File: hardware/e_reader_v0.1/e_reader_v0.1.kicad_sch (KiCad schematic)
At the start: 6 parts, among them J1 SD_Card, J2 Waveshare_7.5_EPD, J3 5Way_Joystick, U1 ESP32-S3-DevKitC

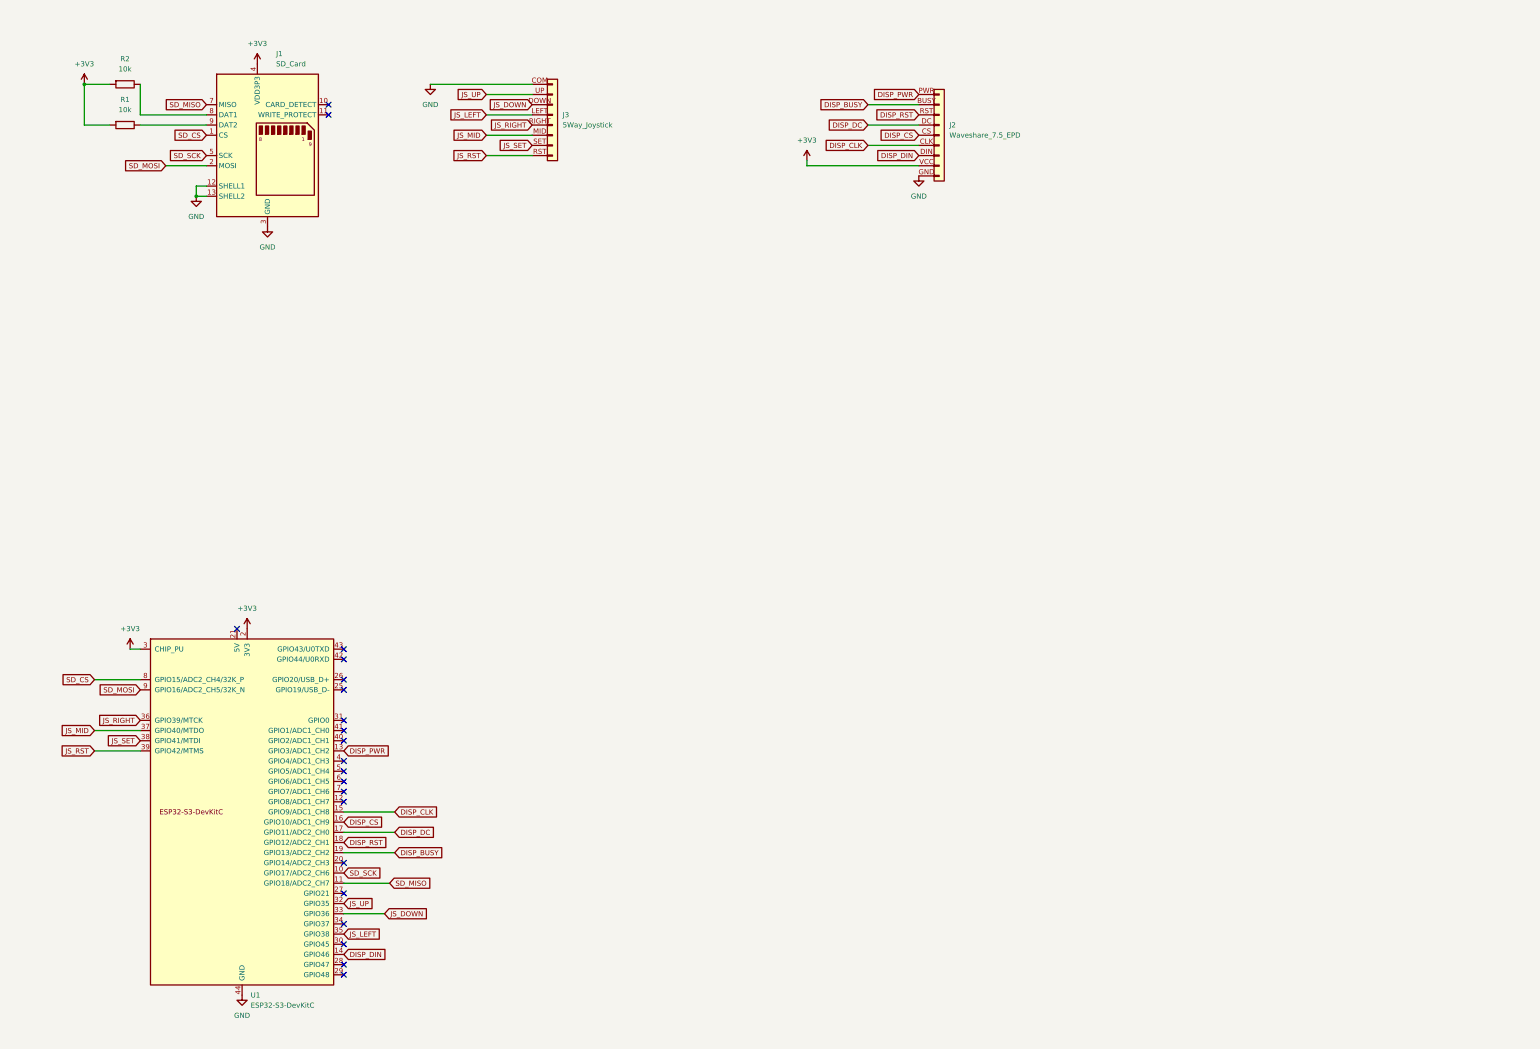
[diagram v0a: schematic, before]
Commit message: Add schematic v0.1 with power, display, SD, buttons, USB-C, LiPo charging
Co-Authored-By: Claude Sonnet 4.6 <noreply@anthropic.com>
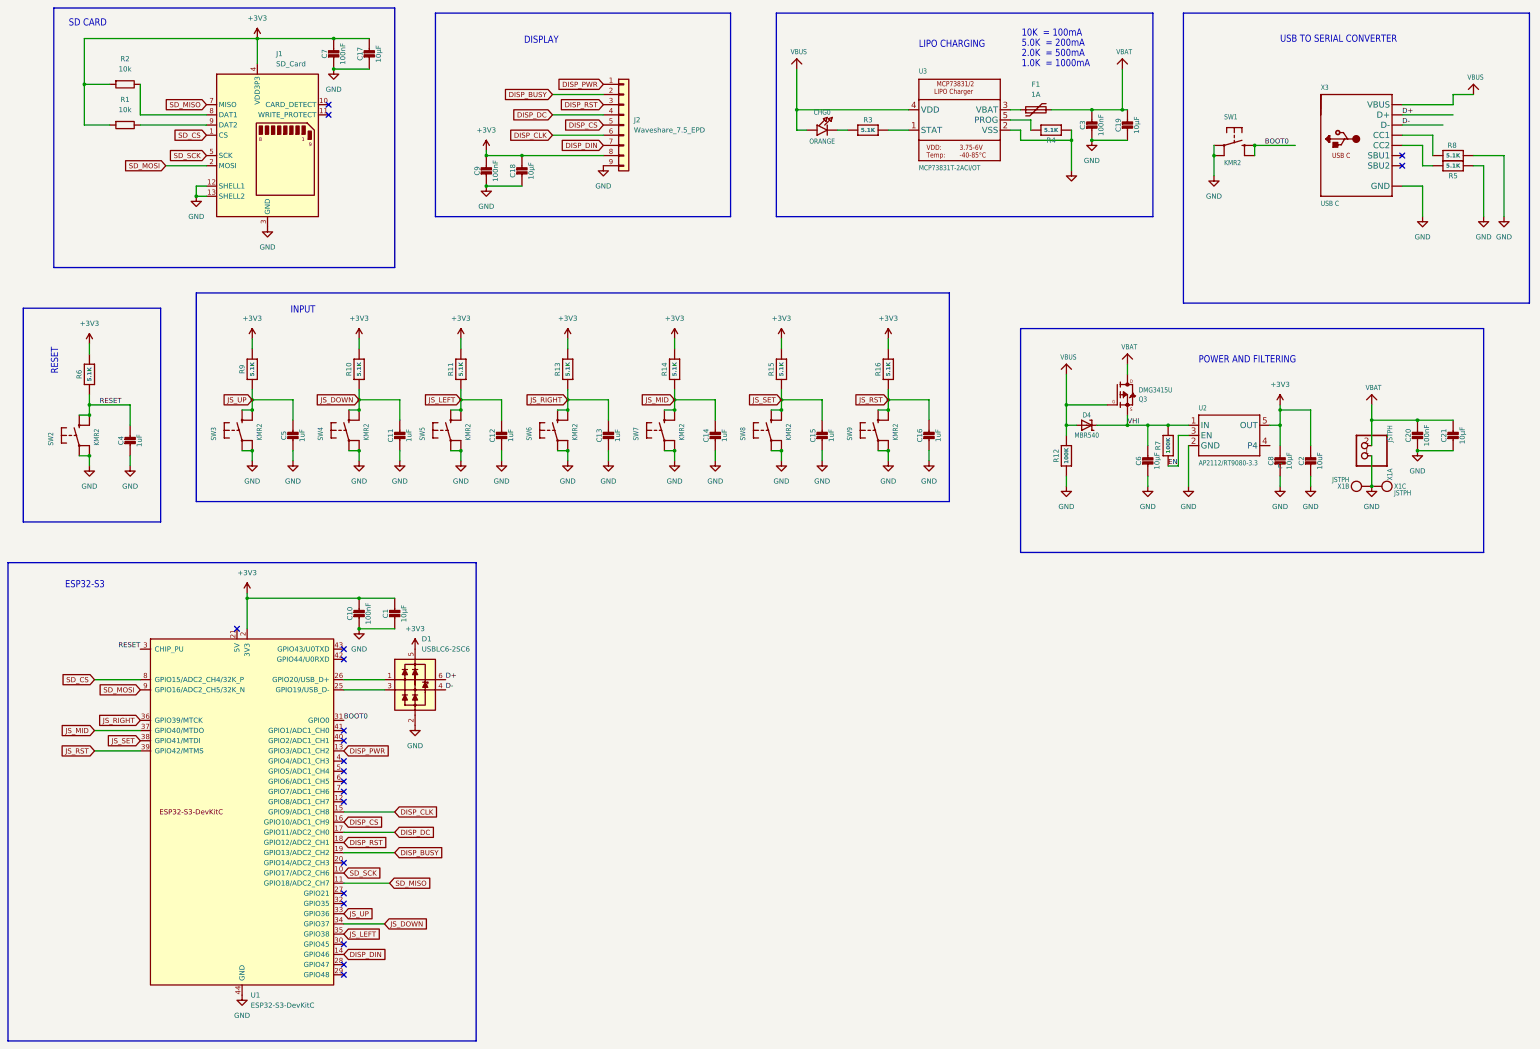
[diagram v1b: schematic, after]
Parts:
- removed J2: Waveshare_7.5_EPD, symbol Connector_Generic:Conn_01x08
- removed J3: 5Way_Joystick, symbol Connector_Generic:Conn_01x08
- added C1, C17, C18, C19, C21: 10µF, Adafruit ESP32-S3 8MB No PSRAM:0603-NO, symbol Adafruit ESP32-S3 8MB No PSRAM-eagle-import:CAP_CERAMIC0603_NO
- added C10, C20, C3, C7, C9: 100nF, Adafruit ESP32-S3 8MB No PSRAM:0603-NO, symbol Adafruit ESP32-S3 8MB No PSRAM-eagle-import:CAP_CERAMIC0603_NO
- added C11, C12, C13, C14, C15, C16, C4, C5: 1uF, Adafruit ESP32-S3 8MB No PSRAM:0603-NO, symbol Adafruit ESP32-S3 8MB No PSRAM-eagle-import:CAP_CERAMIC0603_NO
- added C2: 10uF, Adafruit ESP32-S3 8MB No PSRAM:0805-NO, symbol Adafruit ESP32-S3 8MB No PSRAM-eagle-import:CAP_CERAMIC0805-NOOUTLINE
- added C6, C8: 10µF, Adafruit ESP32-S3 8MB No PSRAM:0805-NO, symbol Adafruit ESP32-S3 8MB No PSRAM-eagle-import:CAP_CERAMIC0805-NOOUTLINE
- added CHG0: ORANGE, Adafruit ESP32-S3 8MB No PSRAM:CHIPLED_0603_NOOUTLINE, symbol Adafruit ESP32-S3 8MB No PSRAM-eagle-import:LED0603_NOOUTLINE
- added D1: USBLC6-2SC6, PCM_Package_TO_SOT_SMD_AKL:SOT-23-6, symbol PCM_Diode_TVS_AKL:USBLC6-2SC6
- added D4: MBR540, Adafruit ESP32-S3 8MB No PSRAM:SOD-123, symbol Adafruit ESP32-S3 8MB No PSRAM-eagle-import:DIODE-SCHOTTKYSOD-123
- added F1: 1A, symbol Device:Polyfuse
- added J2: Waveshare_7.5_EPD, 4ms_Connector:Pins_1x09_2.54mm_TH, symbol PCM_4ms_Connector:Conn_01x09
- added Q3: DMG3415U, Adafruit ESP32-S3 8MB No PSRAM:SOT23-R, symbol Adafruit ESP32-S3 8MB No PSRAM-eagle-import:MOSFET-P
- added R10, R11, R13, R14, R15, R16, R3, R4, R5, R6, R8, R9: 5.1K, Adafruit ESP32-S3 8MB No PSRAM:0603-NO, symbol Adafruit ESP32-S3 8MB No PSRAM-eagle-import:RESISTOR_0603_NOOUT
- added R12, R7: 100K, Adafruit ESP32-S3 8MB No PSRAM:0603-NO, symbol Adafruit ESP32-S3 8MB No PSRAM-eagle-import:RESISTOR_0603_NOOUT
- added SW1, SW2, SW3, SW4, SW5, SW6, SW7, SW8, SW9: KMR2, Adafruit ESP32-S3 8MB No PSRAM:BTN_KMR2_4.6X2.8, symbol Adafruit ESP32-S3 8MB No PSRAM-eagle-import:SWITCH_TACT_SMT4.6X2.8
- added U2: AP2112/RT9080-3.3, Adafruit ESP32-S3 8MB No PSRAM:SOT23-5, symbol Adafruit ESP32-S3 8MB No PSRAM-eagle-import:VREG_SOT23-5
- added U3: MCP73831T-2ACI/OT, Adafruit ESP32-S3 8MB No PSRAM:SOT23-5, symbol Adafruit ESP32-S3 8MB No PSRAM-eagle-import:MCP73831/2
- added X1: JSTPH, Adafruit ESP32-S3 8MB No PSRAM:JSTPH2_BATT, symbol Adafruit ESP32-S3 8MB No PSRAM-eagle-import:CON_JST_PH_2PIN_MT_BATT
- added X3: USB C, Adafruit ESP32-S3 8MB No PSRAM:USB_C_CUSB31-CFM2AX-01-X, symbol Adafruit ESP32-S3 8MB No PSRAM-eagle-import:USB_C
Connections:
- net +3V3: now also C1.1, C10.1, C17.1, C18.1, C2.1, C7.1, C8.1, C9.1, D1.5 (VP), J2.8 (VCC), R10.2, R11.2, R13.2, R14.2, R15.2, R16.2, R6.2, R9.2, U2.5 (OUT); no longer U1.3 (CHIP_PU)
- net DISP_BUSY: now also J2.2 (BUSY)
- net DISP_CLK: now also J2.6 (CLK)
- net DISP_CS: now also J2.5 (CS)
- net DISP_DC: now also J2.4 (DC)
- net DISP_DIN: now also J2.7 (DIN)
- net DISP_PWR: now also J2.1 (PWR)
- net DISP_RST: now also J2.3 (RST)
- net GND: now also C1.2, C10.2, C11.2, C12.2, C13.2, C14.2, C15.2, C16.2, C17.2, C18.2, C19.2, C2.2, C20.2, C21.2, C3.2, C4.2, C5.2, C6.2, C7.2, C8.2, C9.2, D1.2 (VN), J2.9 (GND), R12.1, R4.1, R5.1, R8.1, SW1.A (P), SW1.A' (P1), SW2.A (P), SW2.A' (P1), SW3.A (P), SW3.A' (P1), SW4.A (P), SW4.A' (P1), SW5.A (P), SW5.A' (P1), SW6.A (P), SW6.A' (P1), SW7.A (P), SW7.A' (P1), SW8.A (P), SW8.A' (P1), SW9.A (P), SW9.A' (P1), U2.2 (GND), U3.2 (VSS), X1.1, X1.NC1 (P$1), X1.NC2 (P$1), X3.A1B12 (GND), X3.B1A12 (GND)
- net JS_DOWN: now also U1.34 (GPIO37), C11.1, R10.1, SW4.B (S), SW4.B' (S1); no longer U1.33 (GPIO36)
- net JS_LEFT: now also C12.1, R11.1, SW5.B (S), SW5.B' (S1)
- net JS_MID: now also C14.1, R14.1, SW7.B (S), SW7.B' (S1)
- net JS_RIGHT: now also C13.1, R13.1, SW6.B (S), SW6.B' (S1)
- net JS_RST: now also C16.1, R16.1, SW9.B (S), SW9.B' (S1)
- net JS_SET: now also C15.1, R15.1, SW8.B (S), SW8.B' (S1)
- net JS_UP: now also U1.33 (GPIO36), C5.1, R9.1, SW3.B (S), SW3.B' (S1); no longer U1.32 (GPIO35)
- net at U1.25 (GPIO19/USB_D-): now also D1.3 (L2)
- net at U1.26 (GPIO20/USB_D+): now also D1.1 (L1)
- net BOOT0: now reaches U1.31 (GPIO0)
- net BOOT0: now also SW1.B (S), SW1.B' (S1)
- new net: F1.1, U3.3 (VBAT)
- new net: R8.2, X3.A5 (CC1)
- new net: R5.2, X3.B5 (CC2)
- new net: R4.2, U3.5 (PROG)
- new net: CHG0.C, R3.1
- new net: R3.2, U3.1 (STAT)
- new net D+: D1.6 (L1), X3.A6 (D+), X3.B6 (D+)
- new net D-: D1.4 (L2), X3.A7 (D-), X3.B7 (D-)
- new net EN: R7.1, U2.3 (EN)
- new net RESET: C4.1, R6.1, SW2.B (S), SW2.B' (S1), U1.3 (CHIP_PU)
- new net VBAT: C19.1, C20.1, C21.1, C3.1, F1.2, Q3.3 (D), X1.2
- new net VBUS: CHG0.A, D4.A, Q3.1 (G), R12.2, U3.4 (VDD), X3.A4B9 (VBUS), X3.B4A9 (VBUS)
- new net VHI: C6.1, D4.C, Q3.2 (S), R7.2, U2.1 (IN)
- no-connect marks 21 -> 20
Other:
- note added: "1.0K = 1000mA"
- note added: "10K = 100mA"
- note added: "2.0K = 500mA"
- note added: "5.0K = 200mA"
- note added: "DISPLAY"
- note added: "ESP32-S3"
- note added: "INPUT"
- note added: "LIPO CHARGING"
- note added: "POWER AND FILTERING"
- note added: "RESET"
- note added: "SD CARD"
- note added: "USB TO SERIAL CONVERTER"

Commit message: Switch U1 to ESP32-S3-WROOM-1, update schematic components
- Replace ESP32-S3-DevKitC with WROOM-1 module symbol
- Swap D4 MBR540 (through-hole) for SS54 (SMA SMD)
- Fix USBLC6 VP pin: connect to VBUS instead of +3V3
- Assign correct footprints to U3 MCP73831, D1 USBLC6

Co-Authored-By: Claude Sonnet 4.6 <noreply@anthropic.com>
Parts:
- removed D4: MBR540, Adafruit ESP32-S3 8MB No PSRAM:SOD-123, symbol Adafruit ESP32-S3 8MB No PSRAM-eagle-import:DIODE-SCHOTTKYSOD-123
- removed U1: ESP32-S3-DevKitC, PCM_Espressif:ESP32-S3-DevKitC, symbol Espressif:ESP32-S3-DevKitC
- added D2: SS54, PCM_Diode_SMD_AKL:D_SMC, symbol PCM_Diode_Schottky_AKL:SS54
- added U1: ESP32-S3-WROOM-1, PCM_Espressif:ESP32-S3-WROOM-1, symbol Espressif:ESP32-S3-WROOM-1
- C1, C17, C18, C19, C21: footprint Adafruit ESP32-S3 8MB No PSRAM:0603-NO -> Capacitor_SMD:C_0805_2012Metric
- C11, C12, C13, C14, C15, C16, C20, C3, C4, C5, C7, C9: footprint Adafruit ESP32-S3 8MB No PSRAM:0603-NO -> Capacitor_SMD:C_0402_1005Metric
- C2, C6: footprint Adafruit ESP32-S3 8MB No PSRAM:0805-NO -> Capacitor_SMD:C_0805_2012Metric
- D1: footprint PCM_Package_TO_SOT_SMD_AKL:SOT-23-6 -> Package_TO_SOT_SMD:SOT-23-6
- F1: footprint (none) -> Fuse:Fuse_1206_3216Metric
- J1: footprint Connector_Card:SD_Kyocera_145638009211859+ -> Connector_Card:microSD_HC_Wuerth_693072010801
- J2: footprint 4ms_Connector:Pins_1x09_2.54mm_TH -> Connector_PinHeader_2.54mm:PinHeader_1x09_P2.54mm_Vertical
- Q3: footprint Adafruit ESP32-S3 8MB No PSRAM:SOT23-R -> Package_TO_SOT_SMD:SOT-23
- R1, R2: footprint Resistor_THT:R_Axial_DIN0207_L6.3mm_D2.5mm_P10.16mm_Horizontal -> Resistor_SMD:R_0402_1005Metric
- R10, R11, R12, R13, R14, R15, R16, R3, R4, R5, R6, R7, R8, R9: footprint Adafruit ESP32-S3 8MB No PSRAM:0603-NO -> Resistor_SMD:R_0402_1005Metric
- SW1, SW2, SW3, SW4, SW5, SW6, SW7, SW8, SW9: footprint Adafruit ESP32-S3 8MB No PSRAM:BTN_KMR2_4.6X2.8 -> Connector_USB:USB_C_Receptacle_HRO_TYPE-C-31-M-12
- U2, U3: footprint Adafruit ESP32-S3 8MB No PSRAM:SOT23-5 -> Package_TO_SOT_SMD:SOT-23-5
- X1: footprint Adafruit ESP32-S3 8MB No PSRAM:JSTPH2_BATT -> Connector_JST:JST_PH_B2B-PH-K_1x02_P2.00mm_Vertical
- X3: footprint Adafruit ESP32-S3 8MB No PSRAM:USB_C_CUSB31-CFM2AX-01-X -> Connector_USB:USB_C_Receptacle_HRO_TYPE-C-31-M-12
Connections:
- net +3V3: now also U1.2 (3V3); no longer D1.5 (VP)
- net BOOT0: now also U1.27 (GPIO0/BOOT)
- net DISP_BUSY: now also U1.21 (GPIO13/TOUCH13/ADC2_CH2/FSPIQ/FSPIIO7/SUBSPIQ)
- net DISP_CLK: now also U1.17 (GPIO9/TOUCH9/ADC1_CH8/FSPIHD/SUBSPIHD)
- net DISP_CS: now also U1.18 (GPIO10/TOUCH10/ADC1_CH9/FSPICS0/FSPIIO4/SUBSPICS0)
- net DISP_DC: now also U1.19 (GPIO11/TOUCH11/ADC2_CH0/FSPID/FSPIIO5/SUBSPID)
- net DISP_DIN: now also U1.16 (GPIO46)
- net DISP_PWR: now also U1.15 (GPIO3/TOUCH3/ADC1_CH2)
- net DISP_RST: now also U1.20 (GPIO12/TOUCH12/ADC2_CH1/FSPICLK/FSPIIO6/SUBSPICLK)
- net GND: now also R4.2, R8.2, U1.1 (GND), U1.40 (GND), U1.41 (GND); no longer R4.1, R8.1
- net JS_DOWN: now also U1.30 (SPIDQS/GPIO37/FSPIQ/SUBSPIQ)
- net JS_LEFT: now also U1.31 (GPIO38/FSPIWP/SUBSPIWP)
- net JS_MID: now also U1.33 (MTDO/GPIO40/CLK_OUT2)
- net JS_RIGHT: now also U1.32 (MTCK/GPIO39/CLK_OUT3/SUBSPICS1)
- net JS_RST: now also U1.35 (MTMS/GPIO42)
- net JS_SET: now also U1.34 (MTDI/GPIO41/CLK_OUT1)
- net JS_UP: now also U1.29 (SPIIO7/GPIO36/FSPICLK/SUBSPICLK)
- net RESET: now also U1.3 (EN)
- net SD_CS: now also U1.8 (GPIO15/U0RTS/ADC2_CH4/XTAL_32K_P)
- net SD_MISO: now also U1.11 (GPIO18/U1RXD/ADC2_CH7/CLK_OUT3)
- net SD_MOSI: now also U1.9 (GPIO16/U0CTS/ADC2_CH5/XTAL_32K_N)
- net SD_SCK: now also U1.10 (GPIO17/U1TXD/ADC2_CH6)
- net VBUS: now also D1.5 (VP), D2.2 (A)
- net VHI: now also D2.1 (K)
- net at D1.1 (L1): now also U1.14 (GPIO20/U1CTS/ADC2_CH9/CLK_OUT1/USB_D+)
- net at D1.3 (L2): now also U1.13 (GPIO19/U1RTS/ADC2_CH8/CLK_OUT2/USB_D-)
- net at X3.A5 (CC1): now also R8.1; no longer R8.2
- net at U3.5 (PROG): now also R4.1; no longer R4.2
- net at R3.1: now also U3.1 (STAT); no longer CHG0.C
- net at R3.2: now also CHG0.C; no longer U3.1 (STAT)
- no-connect marks 20 -> 19
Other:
- company: (none) -> robertengineer.com
- moved on the sheet: C1, C10, D1
